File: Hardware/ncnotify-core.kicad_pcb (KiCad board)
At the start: 4 copper layers, 43.4 x 21 mm, 51 parts, among them J1 BNC5-J-P-GN-RA-BH2D, J2 Conn_ARM_JTAG_SWD_10, J3 USB4110-GF-A, SW1 SW_Push, SW2 SW_Push, U1 STM32L422CBT6, U2 TLV71333PDBV, U3 USBLC6-2SC6, U4 USBLC6-2SC6, Y1 Q13FC1350000400

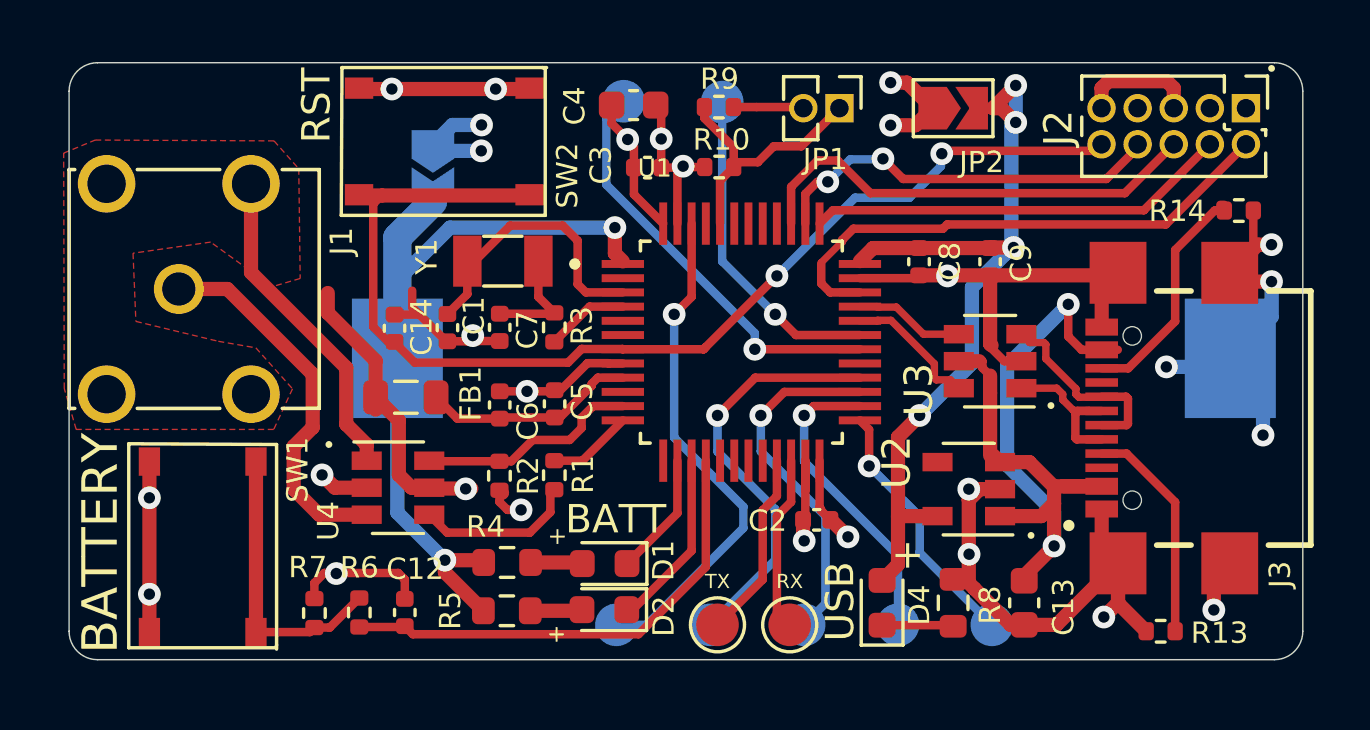
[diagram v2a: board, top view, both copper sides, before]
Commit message: add zener option for power flexibility
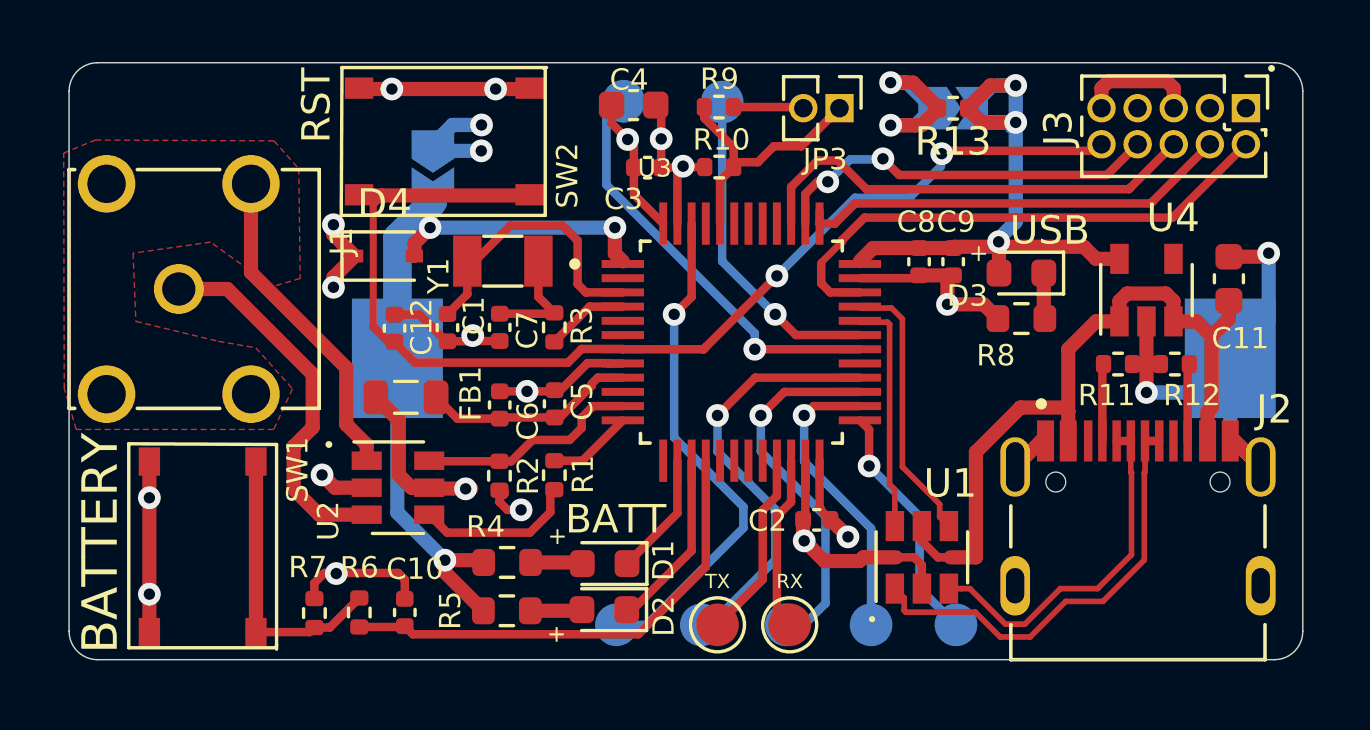
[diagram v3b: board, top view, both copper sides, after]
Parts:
- removed the J3 at (247.0, -37.5)
- removed R14: 5k1, Resistor_SMD:R_0402_1005Metric
- removed the U3 at (242.0, -39.5)
- added D4: D_Schottky, Diode_SMD:D_SOD-323, F.Cu at (220.7, -43.2)
- added J2: TYPE-C-31-M-12, libs:HRO_TYPE-C-31-M-12, F.Cu at (247.2, -31.6)
- added R11: 5k1, Resistor_SMD:R_0402_1005Metric, F.Cu at (246.5, -39.4)
- added R12: 5k1, Resistor_SMD:R_0402_1005Metric, F.Cu at (248.5, -39.4)
- added U1: USBLC6-2SC6, Package_TO_SOT_SMD:SOT-23-6, F.Cu at (239.6, -32.6)
- JP1: renamed from JP2; moved to B.Cu
- R13: value 5k1 -> 0
- TP1: renamed from CS_0; footprint libs:TestPoint_Pad_D1.5mm_No_Ctrd -> TestPoint:TestPoint_Pad_D1.5mm
- TP2: renamed from CS_1; footprint libs:TestPoint_Pad_D1.5mm_No_Ctrd -> TestPoint:TestPoint_Pad_D1.5mm
- TP3: renamed from COPI; footprint libs:TestPoint_Pad_D1.5mm_No_Ctrd -> TestPoint:TestPoint_Pad_D1.5mm
- TP4: renamed from CIPO; footprint libs:TestPoint_Pad_D1.5mm_No_Ctrd -> TestPoint:TestPoint_Pad_D1.5mm
- TP5: renamed from TP1; footprint libs:TestPoint_Pad_D1.5mm_No_Ctrd -> TestPoint:TestPoint_Pad_D1.5mm
- TP6: renamed from TP2; footprint libs:TestPoint_Pad_D1.5mm_No_Ctrd -> TestPoint:TestPoint_Pad_D1.5mm
- TP7: renamed from SCK; footprint libs:TestPoint_Pad_D1.5mm_No_Ctrd -> TestPoint:TestPoint_Pad_D1.5mm
- TP8: renamed from TP7; footprint libs:TestPoint_Pad_D1.5mm_No_Ctrd -> TestPoint:TestPoint_Pad_D1.5mm
- TP9: renamed from TP8; footprint libs:TestPoint_Pad_D1.5mm_No_Ctrd -> TestPoint:TestPoint_Pad_D1.5mm
- moved R13 19.8 mm to (240.7, -48.4)
- moved C11 13.5 mm to (250.4, -42.4), turned to 90 degrees
- moved D3 12.6 mm to (243.1, -42.6), turned to 180 degrees
- moved R8 10.3 mm to (243.1, -41.0), turned to 180 degrees
- moved U4 9.38 mm to (247.5, -42.0), turned to 90 degrees
- moved C9 1.30 mm to (240.7, -43.0)
- moved TP1 1.26 mm to (240.8, -30.2)
- moved TP7 0.95 mm to (237.8, -30.2)
- moved TP4 0.63 mm to (234.8, -30.2)
- moved TP3 0.32 mm to (231.8, -30.2)
- renumbered C12 to C10, C13 to C11, C14 to C12, D4 to D3, J2 to J3, JP3 to JP2, JP1 to JP3, U4 to U2, U1 to U3, U2 to U4
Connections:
- R13 pad 1: Net-(J3-PadA5) -> VBUS
- R13 pad 2: GND -> VDD
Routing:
- net GND: track 94.8 -> 76.1 mm, vias 19 -> 13
- net CONN_D-: track 6.05 -> 15.6 mm
- net Net-(J3-PadB5): track 8.22 -> 0.00 mm
- net Net-(J3-PadA5): track 7.83 -> 0.00 mm
- net D+: track 3.88 -> 10.2 mm
- net CONN_D+: track 6.94 -> 12.5 mm
- net VBUS: track 29.2 -> 24.0 mm, vias 4 -> 3
- net D-: track 4.77 -> 8.91 mm
- net VUSB: track 29.7 -> 26.1 mm, vias 2 -> 0
- net Net-(J2-PadB5): track 0.00 -> 2.73 mm
- net Net-(J2-PadA5): track 0.00 -> 2.72 mm
- net VDD: track 35.0 -> 37.0 mm, vias 9 -> 11
- net Net-(D3-Pad1): track 2.52 -> 1.62 mm
- net VBAT: track 38.3 -> 38.9 mm, vias 2 -> 3
- net SPI2_SS_0: track 9.12 -> 8.59 mm
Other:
- board text added: "CIPO"
- board text added: "COPI"
- board text added: "CS0"
- board text added: "CS1"
- board text added: "SCL"
- board text added: "SCLK"
- board text added: "SDA"
